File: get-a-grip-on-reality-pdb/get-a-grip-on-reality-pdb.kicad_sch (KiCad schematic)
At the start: 40 parts, among them J14 Conn_01x05_Pin, J15 Battery Connector Bat, U6 BQ25887, U7 TPS54KB20RZRR

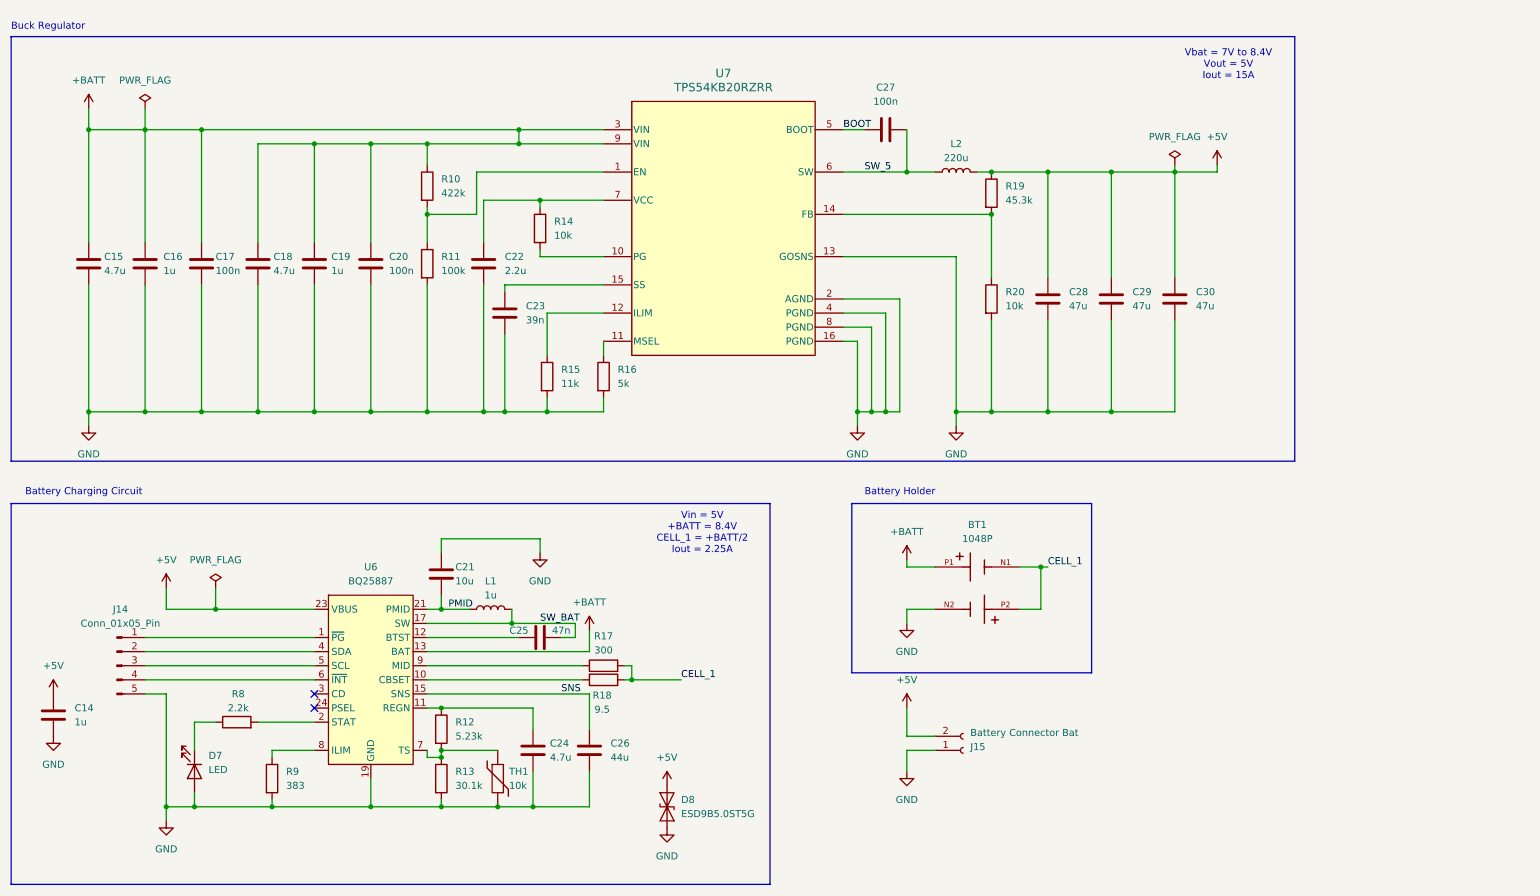
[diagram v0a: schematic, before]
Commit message: add pdb
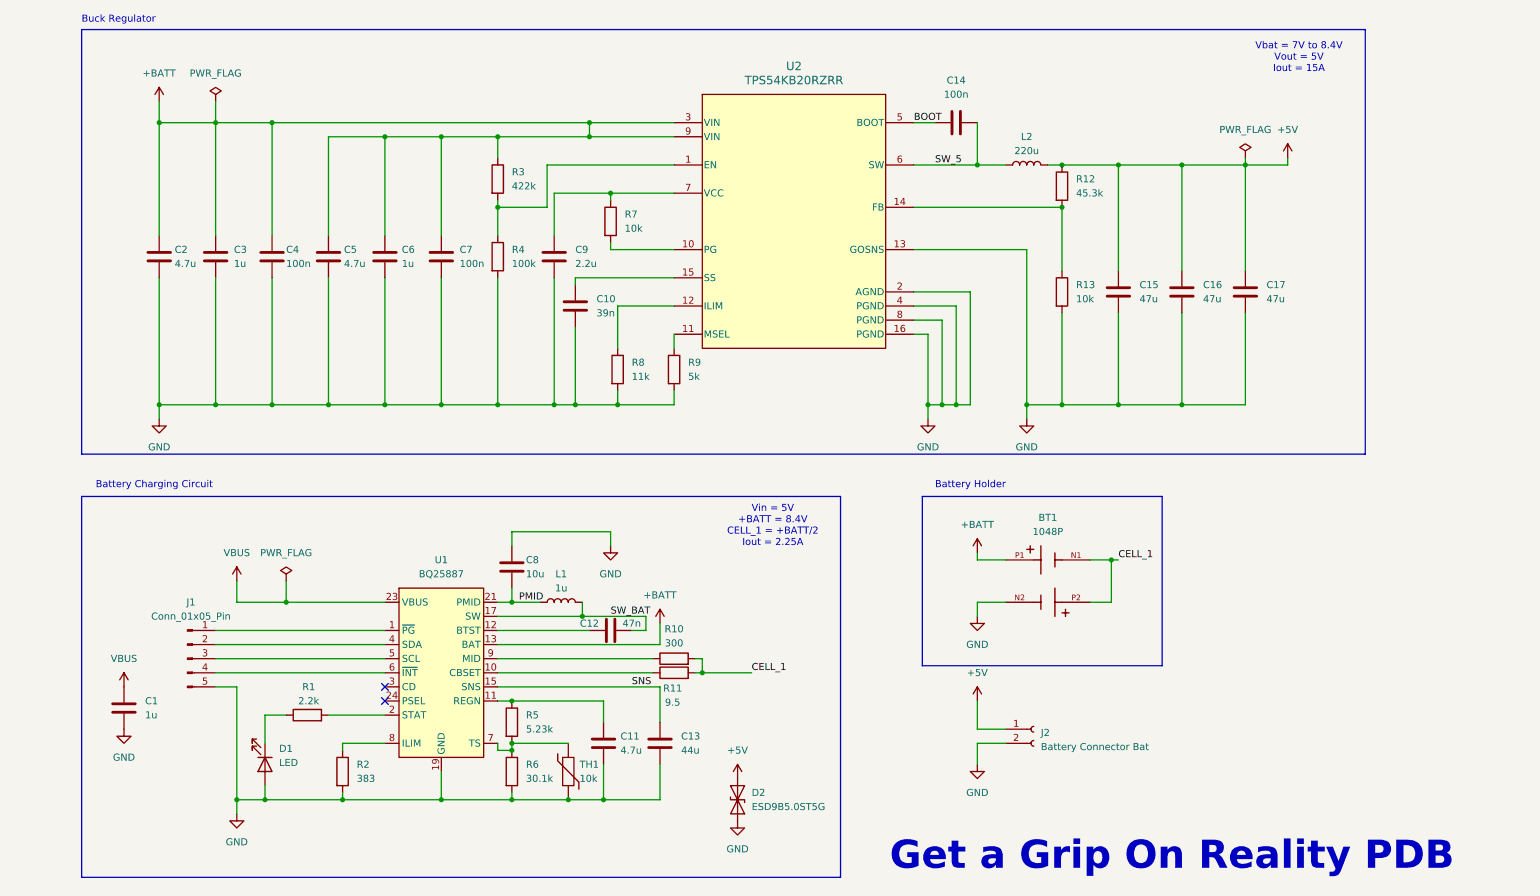
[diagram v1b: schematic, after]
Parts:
- removed C18, C24: 4.7u, Capacitor_SMD:C_0805_2012Metric, symbol Device:C
- removed C19: 1u, Capacitor_SMD:C_0805_2012Metric, symbol Device:C
- removed C20, C27: 100n, Capacitor_SMD:C_0805_2012Metric, symbol Device:C
- removed C21: 10u, Capacitor_SMD:C_0805_2012Metric, symbol Device:C
- removed C22: 2.2u, Capacitor_SMD:C_0805_2012Metric, symbol Device:C
- removed C23: 39n, Capacitor_SMD:C_0805_2012Metric, symbol Device:C
- removed C25: 47n, Capacitor_SMD:C_0805_2012Metric, symbol Device:C
- removed C26: 44u, Capacitor_SMD:C_0805_2012Metric, symbol Device:C
- removed C28, C29, C30: 47u, Capacitor_SMD:C_0805_2012Metric, symbol Device:C
- removed D7: LED, LED_SMD:LED_0805_2012Metric, symbol Device:LED
- removed D8: ESD9B5.0ST5G, Diode_SMD:D_SOD-923, symbol Diode:ESD9B5.0ST5G
- removed J14: Conn_01x05_Pin, Connector_PinHeader_2.54mm:PinHeader_1x05_P2.54mm_Vertical, symbol Connector:Conn_01x05_Pin
- removed J15: Battery Connector Bat, Connector_AMASS:AMASS_XT30PW-F_1x02_P2.50mm_Horizontal, symbol Connector:Conn_01x02_Socket
- removed R14, R20: 10k, Resistor_SMD:R_0805_2012Metric, symbol Device:R
- removed R15: 11k, Resistor_SMD:R_0805_2012Metric, symbol Device:R
- removed R16: 5k, Resistor_SMD:R_0805_2012Metric, symbol Device:R
- removed R17: 300, Resistor_SMD:R_0805_2012Metric, symbol Device:R
- removed R18: 9.5, Resistor_SMD:R_0805_2012Metric, symbol Device:R
- removed R19: 45.3k, Resistor_SMD:R_0805_2012Metric, symbol Device:R
- removed U6: BQ25887, Package_DFN_QFN:VQFN-24-1EP_4x4mm_P0.5mm_EP2.5x2.5mm, symbol Battery_Management:BQ25887
- removed U7: TPS54KB20RZRR, fydp library:RZR0016A-MFG, symbol 2024-06-26_16-50-44:TPS54KB20RZRR
- added C1, C3, C6: 1u, Capacitor_SMD:C_0805_2012Metric, symbol Device:C
- added C10: 39n, Capacitor_SMD:C_0805_2012Metric, symbol Device:C
- added C11, C2, C5: 4.7u, Capacitor_SMD:C_0805_2012Metric, symbol Device:C
- added C12: 47n, Capacitor_SMD:C_0805_2012Metric, symbol Device:C
- added C13: 44u, Capacitor_SMD:C_0805_2012Metric, symbol Device:C
- added C4, C7: 100n, Capacitor_SMD:C_0805_2012Metric, symbol Device:C
- added C8: 10u, Capacitor_SMD:C_0805_2012Metric, symbol Device:C
- added C9: 2.2u, Capacitor_SMD:C_0805_2012Metric, symbol Device:C
- added D1: LED, LED_SMD:LED_0805_2012Metric, symbol Device:LED
- added D2: ESD9B5.0ST5G, Diode_SMD:D_SOD-923, symbol Diode:ESD9B5.0ST5G
- added J1: Conn_01x05_Pin, Connector_PinHeader_2.54mm:PinHeader_1x05_P2.54mm_Vertical, symbol Connector:Conn_01x05_Pin
- added J2: Battery Connector Bat, Connector_AMASS:AMASS_XT30PW-F_1x02_P2.50mm_Horizontal, symbol Connector:Conn_01x02_Socket
- added R1: 2.2k, Resistor_SMD:R_0805_2012Metric, symbol Device:R
- added R2: 383, Resistor_SMD:R_0805_2012Metric, symbol Device:R
- added R3: 422k, Resistor_SMD:R_0805_2012Metric, symbol Device:R
- added R4: 100k, Resistor_SMD:R_0805_2012Metric, symbol Device:R
- added R5: 5.23k, Resistor_SMD:R_0805_2012Metric, symbol Device:R
- added R6: 30.1k, Resistor_SMD:R_0805_2012Metric, symbol Device:R
- added R7: 10k, Resistor_SMD:R_0805_2012Metric, symbol Device:R
- added U1: BQ25887, Package_DFN_QFN:VQFN-24-1EP_4x4mm_P0.5mm_EP2.5x2.5mm, symbol Battery_Management:BQ25887
- added U2: TPS54KB20RZRR, fydp library:RZR0016A-MFG, symbol 2024-06-26_16-50-44:TPS54KB20RZRR
- C14: value 1u -> 100n
- C15: value 4.7u -> 47u
- C16: value 1u -> 47u
- C17: value 100n -> 47u
- R10: value 422k -> 300
- R11: value 100k -> 9.5
- R12: value 5.23k -> 45.3k
- R13: value 30.1k -> 10k
- R8: value 2.2k -> 11k
- R9: value 383 -> 5k
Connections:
- net +5V: now also C15.1, C16.1, C17.1, R12.1, D2.2 (A2), J2.1 (Pin_1); no longer C14.1
- net +BATT: now also C2.1, C3.1, C4.1, C5.1, C6.1, C7.1, R3.1, U1.13 (BAT), U1.14 (BAT), U2.3 (VIN), U2.9 (VIN); no longer C15.1, C16.1, C17.1, R10.1
- net BOOT: now also C14.1, U2.5 (BOOT)
- net CELL_1: now also R10.2, R11.2
- net GND: now also R8.2, C1.2, C10.2, C11.2, C13.2, C2.2, C3.2, C4.2, C5.2, C6.2, C7.2, C8.1, C9.2, D1.2 (A), D2.1 (A1), J1.5 (Pin_5), J2.2 (Pin_2), R2.2, R4.2, R6.2, U1.19 (GND), U1.20 (GND), U2.13 (GOSNS), U2.16 (PGND), U2.2 (AGND), U2.4 (PGND), U2.8 (PGND); no longer C14.2, R11.2
- net PMID: now also C8.2, U1.21 (PMID), U1.22 (PMID)
- net SNS: now also C13.1, U1.15 (SNS), U1.16 (SNS)
- net SW_5: now also C14.2, U2.6 (SW)
- net SW_BAT: now also C12.2, U1.17 (SW), U1.18 (SW)
- net at R8.1: now also U2.12 (ILIM)
- net at R12.2, R13.1: now also U2.14 (FB); no longer TH1.1
- net at R9.1: now also U2.11 (MSEL)
- net at R11.1: now also U1.10 (CBSET); no longer R10.2
- new net: C9.1, R7.1, U2.7 (VCC)
- new net: J1.1 (Pin_1), U1.1 (~{PG})
- new net: J1.2 (Pin_2), U1.4 (SDA)
- new net: J1.3 (Pin_3), U1.5 (SCL)
- new net: J1.4 (Pin_4), U1.6 (~{INT})
- new net: C11.1, R5.1, U1.11 (REGN)
- new net: R5.2, R6.1, TH1.1, U1.7 (TS)
- new net: R7.2, U2.10 (PG)
- new net: C12.1, U1.12 (BTST)
- new net: R1.2, U1.2 (STAT)
- new net: R2.1, U1.8 (ILIM)
- new net: R10.1, U1.9 (MID)
- new net: R3.2, R4.1, U2.1 (EN)
- new net: C10.1, U2.15 (SS)
- new net: D1.1 (K), R1.1
- new net VBUS: C1.1, U1.23 (VBUS)
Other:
- note added: "Get a Grip On Reality PDB"
- title: Power -> (none)
